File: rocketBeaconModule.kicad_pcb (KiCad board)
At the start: 2 copper layers, 106.4 x 64.3 mm, 80 parts, among them J1 TYPE-C-31-M-12, J2 PWR, J3 GND, P1 AntMount, U1 STM32F401CCU6, U2 CP2102N-Axx-xQFN20, U3 CC1200, X1 40MHz, Y1 16MHz

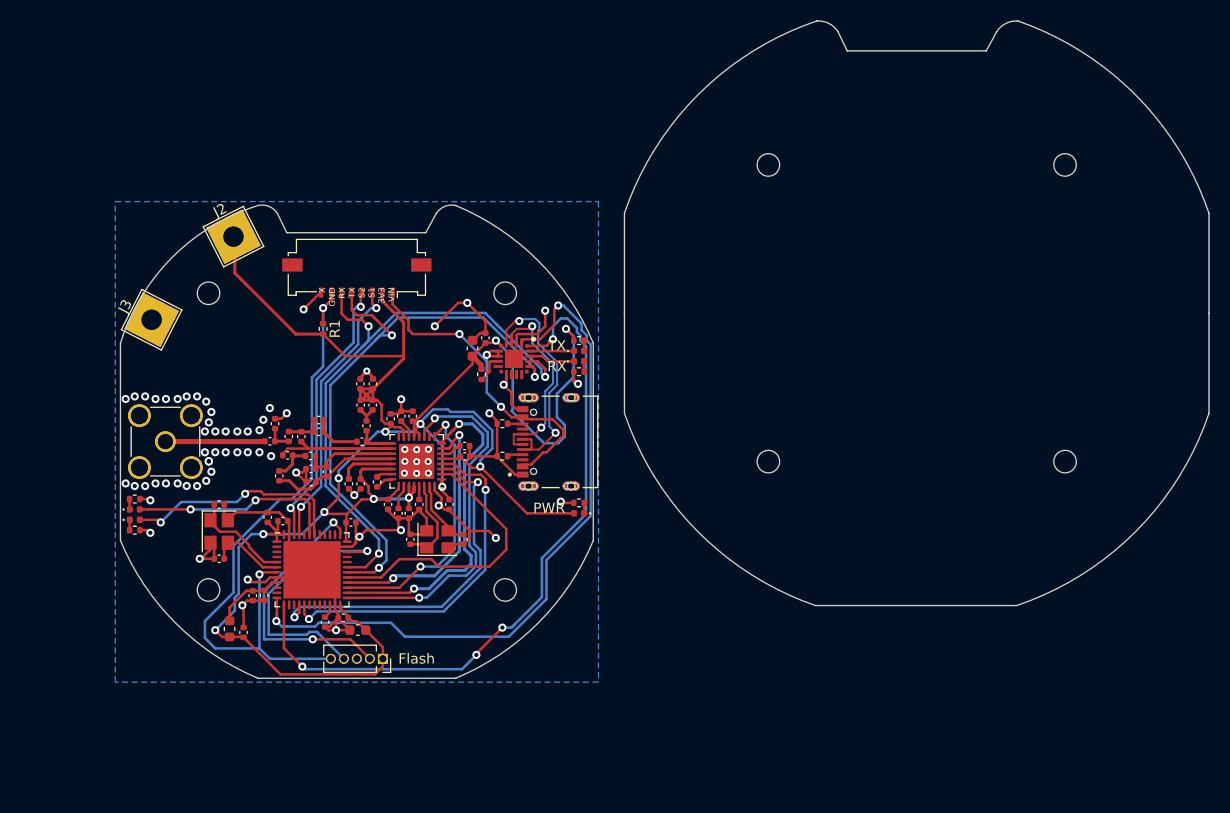
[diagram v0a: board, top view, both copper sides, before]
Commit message: V4 Changes Added SKYWORKS +30db 4W FEM Added LM2576 3.9V supply Increased diameter to 60mm Re-routed full board
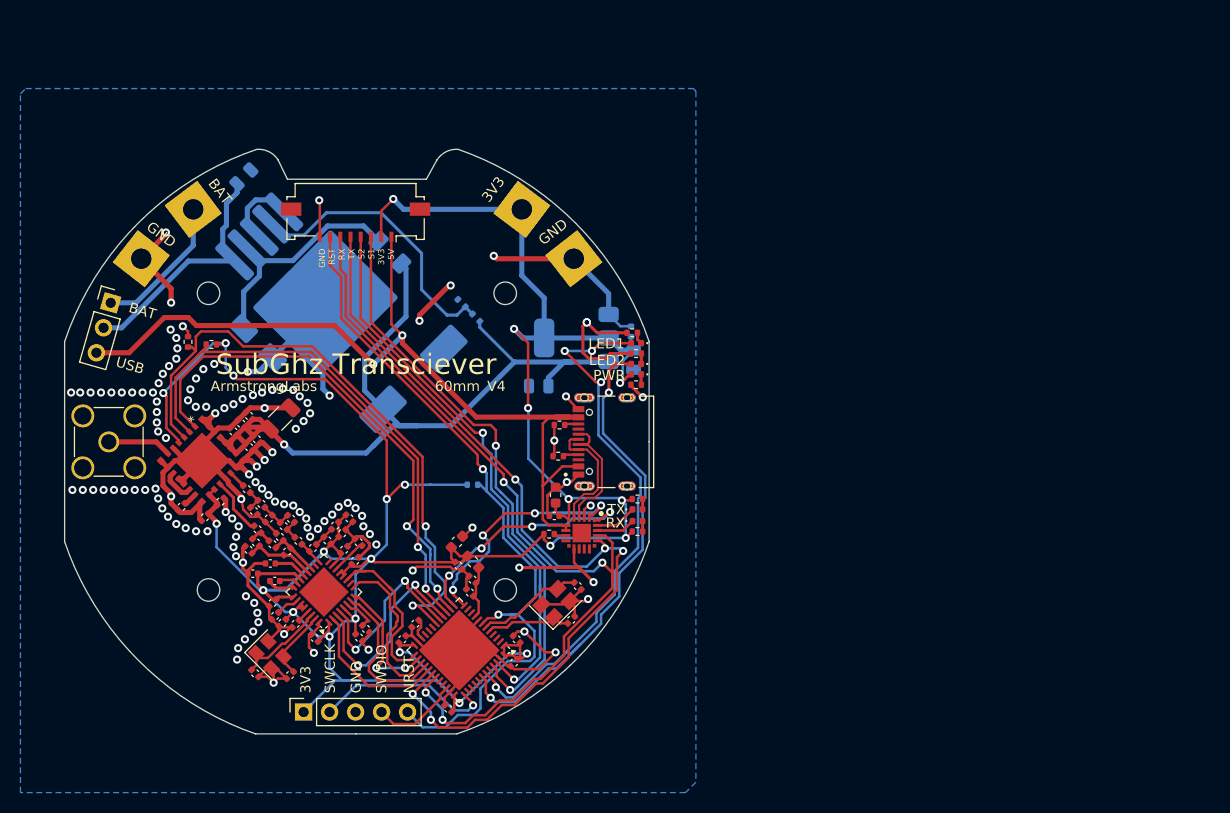
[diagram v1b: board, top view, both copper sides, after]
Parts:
- removed ? (x4): , 
- added C14: 10nF, Capacitor_SMD:C_0402_1005Metric, F.Cu at (58.7, 132.6)
- added C38: 220pF, Capacitor_SMD:C_0402_1005Metric, F.Cu at (57.1, 134.1)
- added C39: 220pF, Capacitor_SMD:C_0402_1005Metric, F.Cu at (61.5, 127.3)
- added C40: 1uF, Capacitor_SMD:C_0402_1005Metric, F.Cu at (59.9, 125.7)
- added C41: 1nF, Capacitor_SMD:C_0402_1005Metric, F.Cu at (60.7, 125.0)
- added C42: 10nF, Capacitor_SMD:C_0402_1005Metric, F.Cu at (62.2, 126.5)
- added C43: 220uF, Capacitor_SMD:C_1206_3216Metric, F.Cu at (64.5, 124.5)
- added C44: 10uF, Capacitor_SMD:C_0402_1005Metric, F.Cu at (61.5, 124.2)
- added C45: 100uF, Capacitor_SMD:C_0805_2012Metric, B.Cu at (61.0, 100.8)
- added C46: 330uF, Capacitor_SMD:CP_Elec_10x10.5, B.Cu at (77.5, 120.6)
- added C47: 22uF, Capacitor_SMD:C_0805_2012Metric, B.Cu at (89.8, 121.3)
- added C48: 22uF, Capacitor_SMD:C_0805_2012Metric, B.Cu at (99.1, 118.7)
- added D6: SS34, Diode_SMD:D_SMA, B.Cu at (62.4, 117.1)
- added J4: PWR, TestPoint:TestPoint_THTPad_4.0x4.0mm_Drill2.0mm, F.Cu at (56.0, 104.0)
- added J5: GND, TestPoint:TestPoint_THTPad_4.0x4.0mm_Drill2.0mm, F.Cu at (50.9, 108.8)
- added J6: Conn_01x03_Pin, Connector_PinHeader_2.54mm:PinHeader_1x03_P2.54mm_Vertical, F.Cu at (47.9, 113.2)
- added R13: 0R, Capacitor_SMD:C_0402_1005Metric, F.Cu at (61.2, 131.4)
- added R14: 1k, Resistor_SMD:R_0402_1005Metric, F.Cu at (57.8, 117.2)
- added R15: 1k, Resistor_SMD:R_0402_1005Metric, F.Cu at (55.5, 117.0)
- added R16: 1.8k, Resistor_SMD:R_0402_1005Metric, B.Cu at (82.2, 113.2)
- added R17: 3.9k, Resistor_SMD:R_0402_1005Metric, B.Cu at (83.7, 114.6)
- added R18: 1k, Resistor_SMD:R_0402_1005Metric, B.Cu at (98.8, 116.0)
- added R2: 0, Capacitor_SMD:C_0402_1005Metric, F.Cu at (54.9, 133.1)
- added U4: SKY65366-21, SKY65366:SKY65366-21_SKY, F.Cu at (56.9, 128.6)
- added U5: LM2576S, Package_TO_SOT_SMD:TO-263-5_TabPin3, B.Cu at (67.9, 112.1)
- added U6: AMS1117-3.3, Package_TO_SOT_SMD:SOT-223-3_TabPin2, B.Cu at (93.5, 116.6)
- J2, J3, R1: moved to B.Cu
- L7: value 43nH -> 22nH
- L8: value 22nH -> 220uH; footprint Capacitor_SMD:C_0402_1005Metric -> Capacitor_SMD:C_1206_3216Metric_Pad1.33x1.80mm_HandSolder; moved to B.Cu
- SWD1: footprint Connector_PinSocket_1.27mm:PinSocket_1x05_P1.27mm_Vertical -> Connector_PinSocket_2.54mm:PinSocket_1x05_P2.54mm_Vertical
- moved R7 52.0 mm to (99.3, 118.1), turned to 180 degrees
- moved D2 51.6 mm to (99.3, 117.1), turned to 180 degrees
- moved D3 51.3 mm to (99.3, 119.1), turned to 180 degrees
- moved R6 51.3 mm to (98.9, 116.1), turned to 180 degrees
- moved J3 41.7 mm to (93.2, 108.8), turned to 128 degrees
- moved C3 36.2 mm to (93.0, 144.1), turned to 45 degrees
- moved C6 35.2 mm to (93.6, 140.8), turned to -45 degrees
- moved Y1 33.6 mm to (91.4, 142.5), turned to 45 degrees
- moved J2 28.3 mm to (88.1, 104.0), turned to 143 degrees
- moved C7 27.1 mm to (87.6, 146.1), turned to 135 degrees
- moved FB1 24.7 mm to (83.4, 138.5), turned to 135 degrees
- moved C12 22.0 mm to (82.0, 138.9), turned to -45 degrees
- moved L8 21.9 mm to (75.2, 108.2), turned to -45 degrees
- moved C11 21.5 mm to (83.3, 140.2), turned to 135 degrees
- moved C36 21.5 mm to (65.5, 149.5), turned to -135 degrees
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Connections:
- net +3.3V renamed FEM_VPC
- C35 pad 1: Net-(C35-Pad1) -> Net-(C34-Pad1)
- C35 pad 2: Net-(C34-Pad1) -> GND
- L6 pad 1: Net-(C35-Pad1) -> Net-(C33-Pad1)
- L6 pad 2: Net-(C33-Pad1) -> Net-(U4-RX0)
- L8 pad 1: Net-(C37-Pad1) -> Net-(D6-K)
- L8 pad 2: Net-(L8-Pad2) -> +3V9
- P1 pad 1: Net-(L8-Pad2) -> Net-(P1-Pin_1)
- U1 pad 14: unconnected-(U1-Pad14) -> FEM_TR
- U1 pad 15: unconnected-(U1-Pad15) -> FEM_EN
- U1 pad 18: unconnected-(U1-Pad18) -> FEM_BYP
- U3 pad 18: Net-(C35-Pad1) -> unconnected-(U3-TRX_SW-Pad18)
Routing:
- net GND: track 128.1 -> 253.3 mm, vias 69 -> 127
- net +3V9: track 0.00 -> 90.6 mm, vias 0 -> 1
- net FEM_VPC: track 228.5 -> 297.5 mm, vias 13 -> 23
- net FEM_BYP: track 0.00 -> 60.6 mm, vias 0 -> 2
- net FEM_EN: track 0.00 -> 52.1 mm, vias 0 -> 2
- net FEM_TR: track 0.00 -> 49.9 mm, vias 0 -> 2
- net VBUS: track 35.1 -> 84.8 mm, vias 3 -> 2
- net /CP2102N_SIG2: track 69.2 -> 24.8 mm
- net /CP2102N_SIG1: track 69.8 -> 28.4 mm, vias 2 -> 4
- net /LED1: track 20.2 -> 54.1 mm, vias 2 -> 4
- net /S1: track 27.2 -> 57.0 mm
- net Net-(U5-FB): track 0.00 -> 29.5 mm
- net /S2: track 26.9 -> 55.7 mm
- net /LED2: track 22.2 -> 48.8 mm
- net /TX: track 59.7 -> 84.4 mm, vias 3 -> 5
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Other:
- board size 106.4 x 64.3 mm -> 57.2 x 57.2 mm
- board text added: "3V3"
- board text added: "60mm"
- board text added: "BAT"
- board text added: "GND"
- board text added: "GND RST RX TX S2 S1 3V3 5V"
- board text added: "LED1"
- board text added: "LED2"
- board text added: "NRST"
- board text added: "SWCLK"
- board text added: "SWDIO"
- board text added: "USB"
- board text added: "V4"
- board text removed: "50mm"
- board text removed: "Flash"
- board text removed: "V3"
- board text removed: "X GND RX TX S2 S1 3V3 VIN"

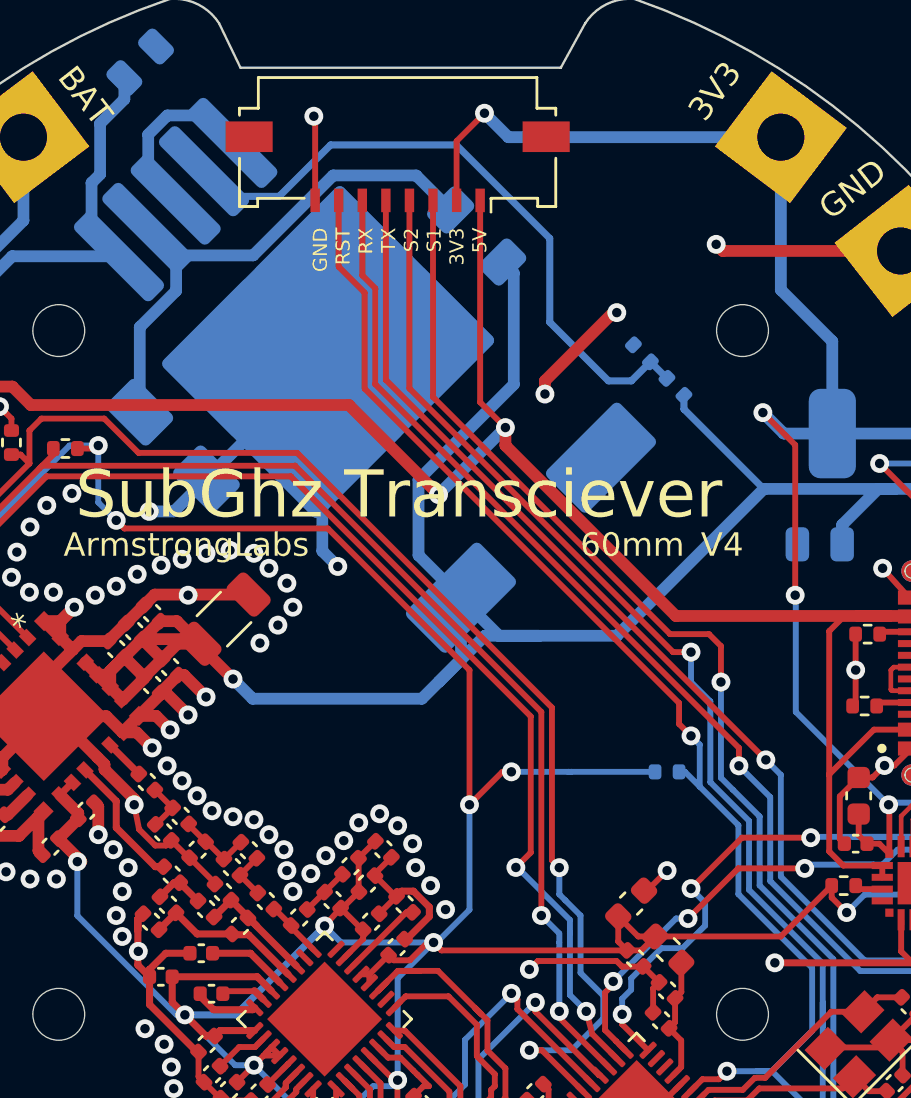
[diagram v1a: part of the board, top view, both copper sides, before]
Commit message: Adjusted some component footprints and part numbers Increased size of inductor and repositioned generated gbrs, drills, bom and cpl (up to date)
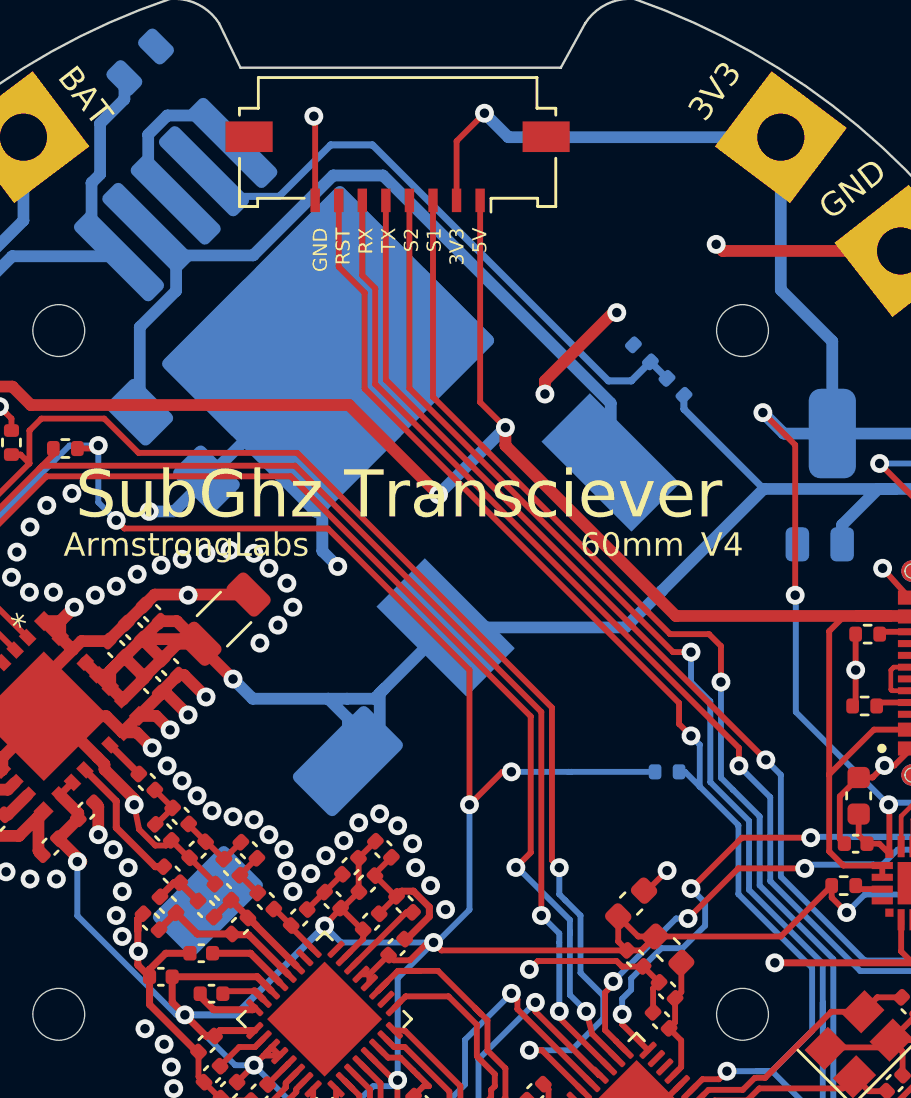
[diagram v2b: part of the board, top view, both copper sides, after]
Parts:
- L8: footprint Capacitor_SMD:C_1206_3216Metric_Pad1.33x1.80mm_HandSolder -> Inductor_SMD:L_Sunlord_SWRB1207S
- moved C46 16.8 mm to (66.8, 133.5), turned to 45 degrees
- moved L8 13.3 mm to (77.4, 121.3), turned to -135 degrees
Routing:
- net +3V9: track 90.6 -> 72.5 mm
- net Net-(D6-K): track 24.3 -> 37.0 mm
- net Net-(U5-FB): track 29.5 -> 27.4 mm

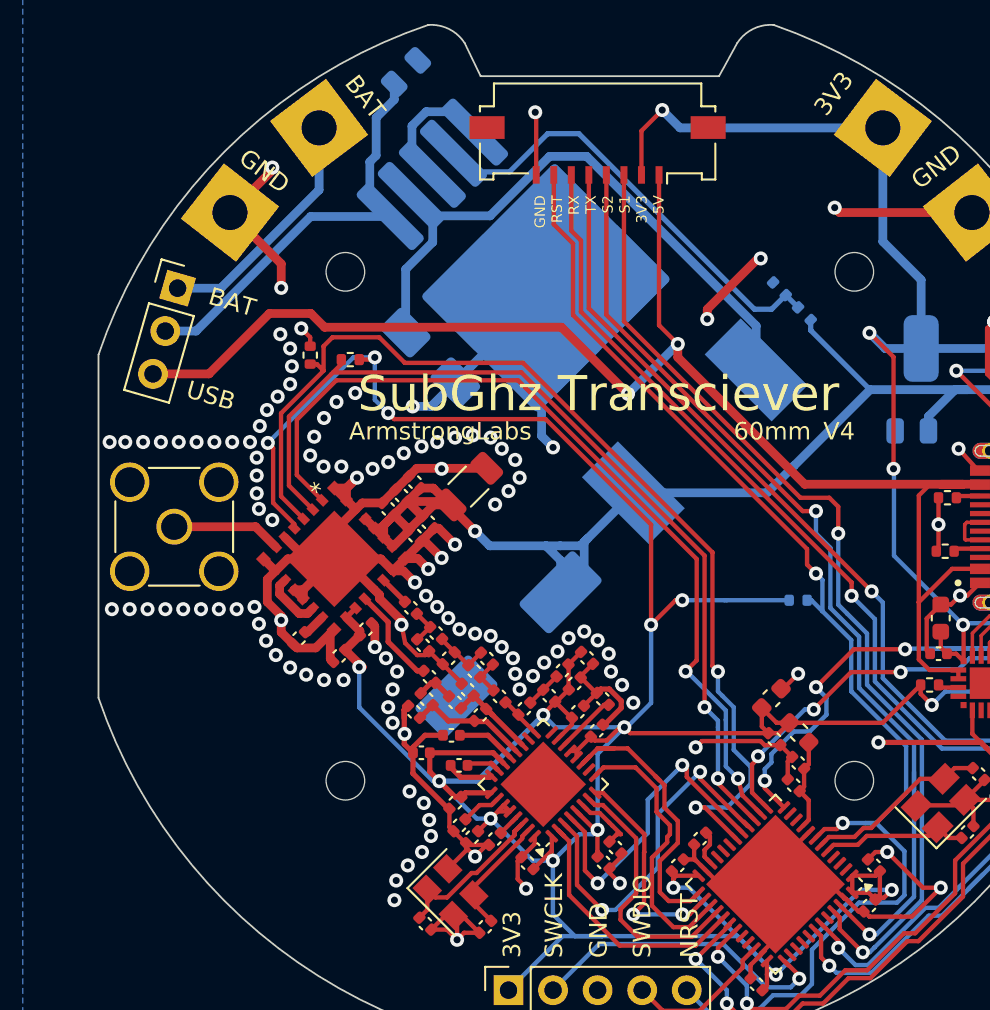
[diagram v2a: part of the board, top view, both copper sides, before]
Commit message: switched pins on ribbon cable to connect evenly with FC when flipped
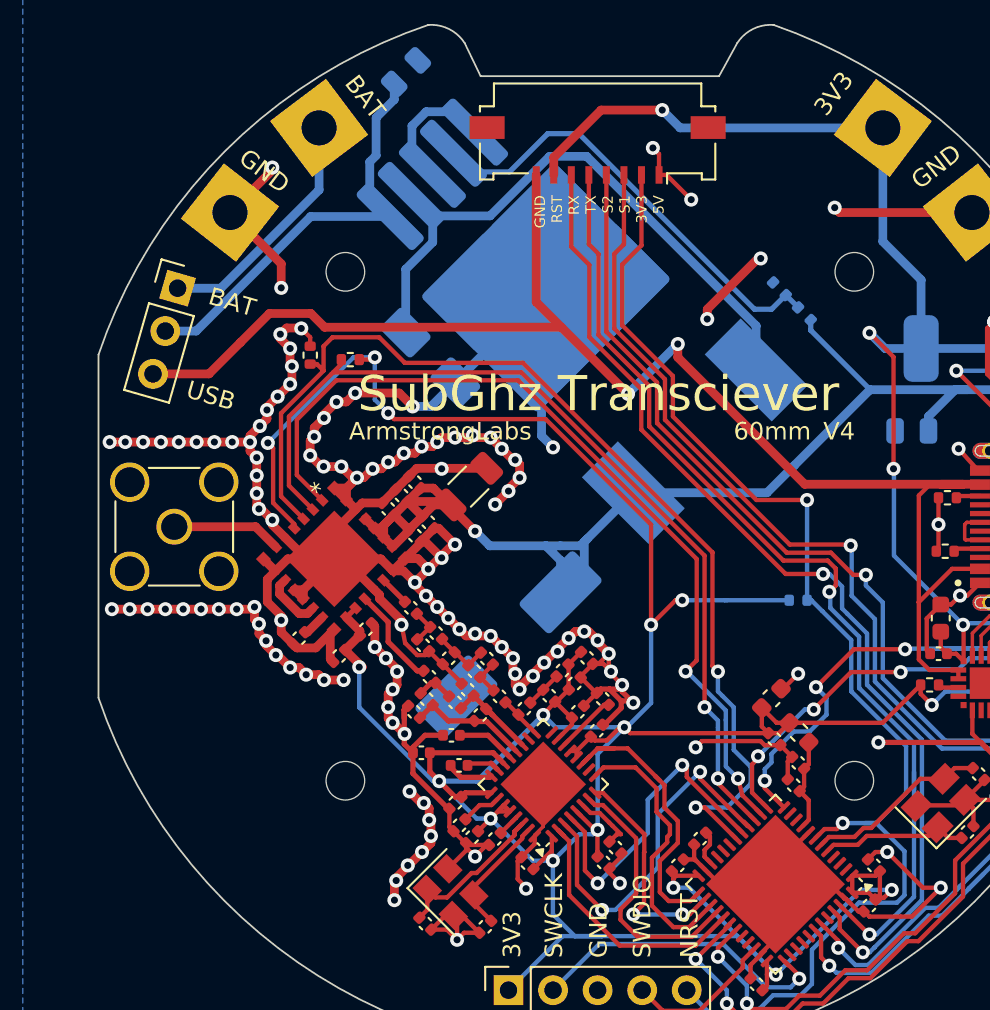
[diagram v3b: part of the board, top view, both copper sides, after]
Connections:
- EX1 pad 1: VBUS -> GND
- EX1 pad 2: FEM_VPC -> /NRST
- EX1 pad 3: /S1 -> /RX
- EX1 pad 4: /S2 -> /TX
- EX1 pad 5: /TX -> /S2
- EX1 pad 6: /RX -> /S1
- EX1 pad 7: /NRST -> FEM_VPC
- EX1 pad 8: GND -> VBUS
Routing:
- net GND: track 253.3 -> 362.0 mm, vias 127 -> 128
- net FEM_VPC: track 297.5 -> 301.6 mm
- net /S2: track 55.7 -> 57.4 mm
- net /S1: track 57.0 -> 58.7 mm
- net /TX: track 84.4 -> 85.9 mm
- net /RX: track 83.5 -> 84.8 mm
- net VBUS: track 84.8 -> 84.0 mm
- net /NRST: track 73.7 -> 73.1 mm

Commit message: removed old PA
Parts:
- removed C46: 330uF, Capacitor_SMD:CP_Elec_10x10.5
- removed C47, C48: 22uF, Capacitor_SMD:C_0805_2012Metric
- removed L8: 220uH, Inductor_SMD:L_Sunlord_SWRB1207S
- removed U5: LM2576S, Package_TO_SOT_SMD:TO-263-5_TabPin3
- removed U6: AMS1117-3.3, Package_TO_SOT_SMD:SOT-223-3_TabPin2
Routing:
- net +3V9: track 72.5 -> 70.7 mm
